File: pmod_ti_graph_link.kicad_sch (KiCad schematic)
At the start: 11 parts, among them J1 Pmod Peripheral, J2 Graph Link, J3 Link Debug, Q1 UMH4N

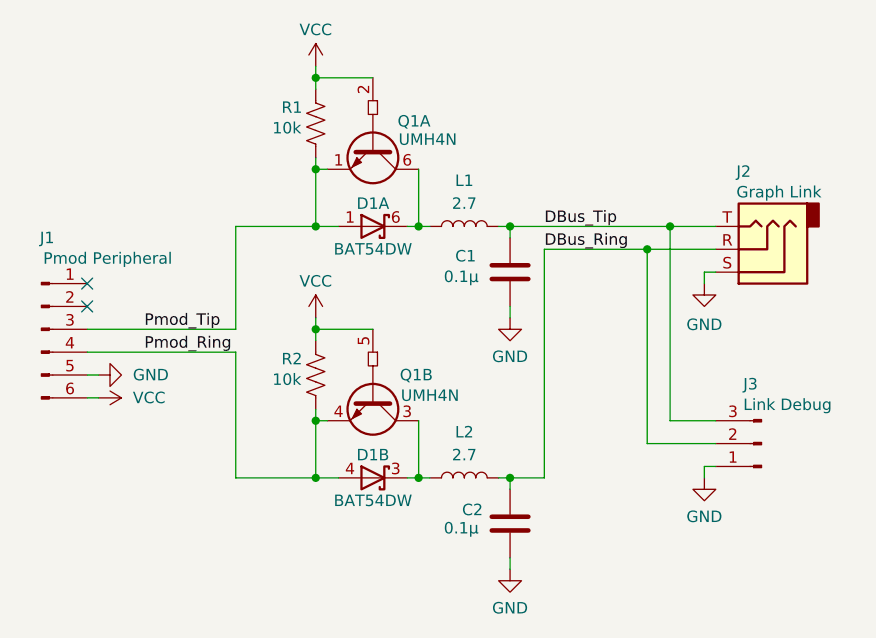
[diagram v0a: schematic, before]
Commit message: Clean up routing, add GND vias, add text
- Clean up routing around transistor and diode
- Add stitching GND vias around perimeter
- Add "Pmod TI Graph Link" text and date
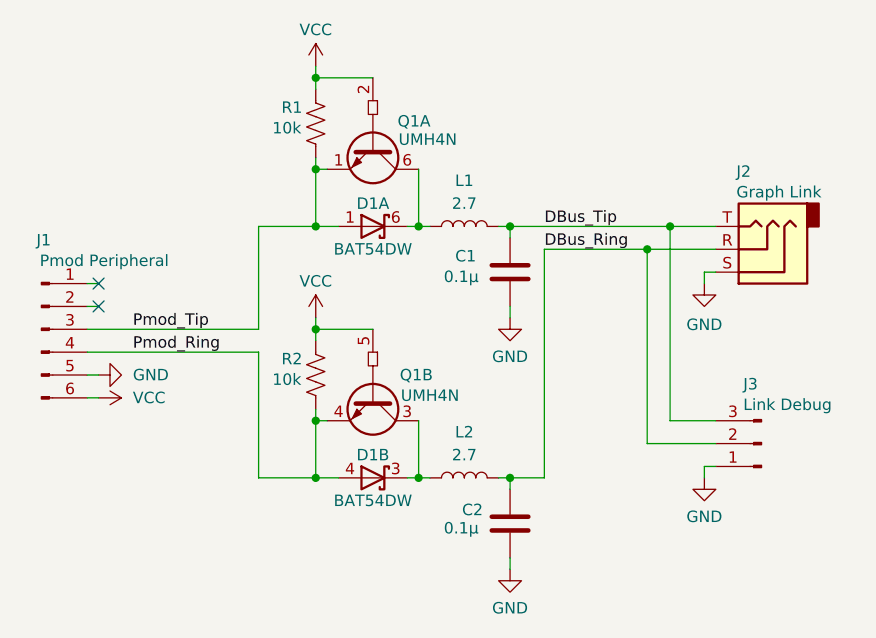
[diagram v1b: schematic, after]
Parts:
- added unit 2 of D1
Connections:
- net Pmod_Ring: now also D1.4 (A); no longer D1.4 (A)
- net at L2.1, Q1.3 (C2): now also D1.3 (K); no longer D1.3 (K)
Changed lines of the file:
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@@
 	)
 	(no_connect
-		(at 68.58 90.17)
+		(at 69.85 87.63)
 	)
 	(no_connect
-		(at 68.58 87.63)
+		(at 69.85 90.17)
 	)
 	(wire
@@
 	(wire
 		(pts
-			(xy 85.09 95.25) (xy 85.09 109.22)
+			(xy 87.63 95.25) (xy 87.63 109.22)
 		)
 		(stroke
@@
 	(wire
 		(pts
-			(xy 68.58 95.25) (xy 85.09 95.25)
+			(xy 68.58 95.25) (xy 87.63 95.25)
 		)
 		(stroke
@@
 	(wire
 		(pts
-			(xy 68.58 92.71) (xy 85.09 92.71)
+			(xy 68.58 92.71) (xy 87.63 92.71)
 		)
 		(stroke
@@
 	(wire
 		(pts
-			(xy 85.09 92.71) (xy 85.09 81.28)
+			(xy 87.63 92.71) (xy 87.63 81.28)
 		)
 		(stroke
@@
 	(wire
 		(pts
-			(xy 85.09 81.28) (xy 93.98 81.28)
+			(xy 87.63 81.28) (xy 93.98 81.28)
 		)
 		(stroke
@@
 	(wire
 		(pts
+			(xy 68.58 87.63) (xy 69.85 87.63)
+		)
+		(stroke
+			(width 0)
+			(type default)
+		)
+	)
+	(wire
+		(pts
 			(xy 137.16 107.95) (xy 137.16 109.22)
 		)
@@
 	(wire
 		(pts
-			(xy 85.09 109.22) (xy 93.98 109.22)
+			(xy 87.63 109.22) (xy 93.98 109.22)
 		)
 		(stroke
@@
 	(wire
 		(pts
+			(xy 68.58 90.17) (xy 69.85 90.17)
+		)
+		(stroke
+			(width 0)
+			(type default)
+		)
+	)
+	(wire
+		(pts
 			(xy 93.98 73.66) (xy 93.98 74.93)
 		)
@@
 	)
 	(label "Pmod_Ring"
-		(at 74.93 95.25 0)
+		(at 73.66 95.25 0)
 		(effects
 			(font
@@
 	)
 	(label "Pmod_Tip"
-		(at 74.93 92.71 0)
+		(at 73.66 92.71 0)
 		(effects
 			(font
@@
 		(dnp no)
 		(property "Reference" "J1"
-			(at 64.135 82.55 0)
+			(at 63.754 82.804 0)
 			(effects
 				(font
@@
 		)
 		(property "Value" "Pmod Peripheral"
-			(at 70.866 84.836 0)
-			(effects
-				(font
+			(at 70.485 85.09 0)
+			(effects
+				(font

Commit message: Add inductor shield->GND and clean up placement and routing. Prelim "Rev A"
- Add optional inductor between 2.5mm shield and GND
- Make VCC thicker, update calc icon, clean up traces
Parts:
- added L3: 2.7, Inductor_SMD:L_1008_2520Metric_Pad1.43x2.20mm_HandSolder, symbol Device:L
- Q1: value UMH4N -> RN1911
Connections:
- net GND: now also L3.1; no longer J2.S
- new net: J2.S, L3.2
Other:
- moved on the sheet: J3
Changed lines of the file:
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@@
 	(wire
 		(pts
-			(xy 133.35 102.87) (xy 133.35 81.28)
+			(xy 133.35 107.95) (xy 133.35 81.28)
 		)
 		(stroke
@@
 	(wire
 		(pts
-			(xy 137.16 107.95) (xy 138.43 107.95)
+			(xy 137.16 113.03) (xy 138.43 113.03)
 		)
 		(stroke
@@
 	(wire
 		(pts
-			(xy 130.81 83.82) (xy 130.81 105.41)
+			(xy 130.81 83.82) (xy 130.81 110.49)
 		)
 		(stroke
@@
 	(wire
 		(pts
+			(xy 137.16 86.36) (xy 137.16 87.63)
+		)
+		(stroke
+			(width 0)
+			(type default)
+		)
+	)
+	(wire
+		(pts
 			(xy 93.98 81.28) (xy 96.52 81.28)
 		)
@@
 	(wire
 		(pts
-			(xy 137.16 107.95) (xy 137.16 109.22)
+			(xy 137.16 113.03) (xy 137.16 114.3)
 		)
 		(stroke
@@
 	(wire
 		(pts
+			(xy 137.16 95.25) (xy 137.16 96.52)
+		)
+		(stroke
+			(width 0)
+			(type default)
+		)
+	)
+	(wire
+		(pts
 			(xy 93.98 64.77) (xy 100.33 64.77)
 		)
@@
 	(wire
 		(pts
-			(xy 133.35 102.87) (xy 138.43 102.87)
-		)
-		(stroke
-			(width 0)
-			(type default)
-		)
-	)
-	(wire
-		(pts
-			(xy 130.81 105.41) (xy 138.43 105.41)
-		)
-		(stroke
-			(width 0)
-			(type default)
-		)
-	)
-	(wire
-		(pts
-			(xy 137.16 87.63) (xy 137.16 86.36)
+			(xy 133.35 107.95) (xy 138.43 107.95)
+		)
+		(stroke
+			(width 0)
+			(type default)
+		)
+	)
+	(wire
+		(pts
+			(xy 130.81 110.49) (xy 138.43 110.49)
 		)
 		(stroke
@@
 	(symbol
 		(lib_id "power:GND")
-		(at 137.16 109.22 0)
+		(at 137.16 114.3 0)
 		(unit 1)
 		(exclude_from_sim no)
@@
 		(dnp no)
 		(property "Reference" "#PWR06"
-			(at 137.16 115.57 0)
+			(at 137.16 120.65 0)
 			(effects
 				(font
@@
 		)
 		(property "Value" "GND"
-			(at 137.16 113.538 0)
+			(at 137.16 118.618 0)
 			(effects
 				(font
@@
 		)
 		(property "Footprint" ""
-			(at 137.16 109.22 0)
+			(at 137.16 114.3 0)
 			(effects
 				(font
@@
 		)
 		(property "Datasheet" ""
-			(at 137.16 109.22 0)
+			(at 137.16 114.3 0)
 			(effects
 				(font
@@
 		)
 		(property "Description" "Power symbol creates a global label with name \"GND\" , ground"
-			(at 137.16 109.22 0)
+			(at 137.16 114.3 0)
 			(effects
 				(font
@@
 				(path "/d64bf880-8167-432e-9a3f-0e567d00bae5"
 					(reference "#PWR06")
+					(unit 1)
+				)
+			)
+		)
+	)
+	(symbol
+		(lib_id "Device:L")
+		(at 137.16 91.44 180)
+		(unit 1)
+		(exclude_from_sim no)
+		(in_bom yes)
+		(on_board yes)
+		(dnp no)
+		(fields_autoplaced yes)
+		(property "Reference" "L3"
+			(at 138.43 90.1699 0)
+			(effects
+				(font
+					(size 1.27 1.27)
+				)
+				(justify right)
+			)
+		)
+		(property "Value" "2.7"
+			(at 138.43 92.7099 0)
+			(effects
+				(font
+					(size 1.27 1.27)
+				)
+				(justify right)
+			)
+		)
+		(property "Footprint" "Inductor_SMD:L_1008_2520Metric_Pad1.43x2.20mm_HandSolder"
+			(at 137.16 91.44 0)
+			(effects
+				(font
+					(size 1.27 1.27)
+				)
+				(hide yes)
+			)
+		)
+		(property "Datasheet" "~"
+			(at 137.16 91.44 0)
+			(effects
+				(font
+					(size 1.27 1.27)
+				)
+				(hide yes)
+			)
+		)
+		(property "Description" "Inductor"
+			(at 137.16 91.44 0)
+			(effects
+				(font
+					(size 1.27 1.27)
+				)
+				(hide yes)
+			)
+		)
+		(pin "1"
+		)
+		(pin "2"
+		)
+		(instances
+			(project "pmod_ti_graph_link"
+				(path "/d64bf880-8167-432e-9a3f-0e567d00bae5"
+					(reference "L3")
 					(unit 1)
 				)
@@
 	(symbol
 		(lib_id "power:GND")
-		(at 137.16 87.63 0)
+		(at 137.16 96.52 0)
 		(unit 1)
 		(exclude_from_sim no)
@@
 		(dnp no)
 		(property "Reference" "#PWR05"
-			(at 137.16 93.98 0)
+			(at 137.16 102.87 0)
 			(effects
 				(font
@@
 		)
 		(property "Value" "GND"
-			(at 137.16 92.202 0)
+			(at 137.16 101.092 0)
 			(effects
 				(font
@@
 		)
 		(property "Footprint" ""
-			(at 137.16 87.63 0)
+			(at 137.16 96.52 0)
 			(effects
 				(font
@@
 		)
 		(property "Datasheet" ""
-			(at 137.16 87.63 0)
+			(at 137.16 96.52 0)
 			(effects
 				(font
@@
 		)
 		(property "Description" "Power symbol creates a global label with name \"GND\" , ground"
-			(at 137.16 87.63 0)
+			(at 137.16 96.52 0)
 			(effects
 				(font
@@
 			)
 		)
-		(property "Value" "UMH4N"
+		(property "Value" "RN1911"
 			(at 106.68 100.076 90)
 			(effects
@@
 			)
 		)
-		(property "Value" "UMH4N"
+		(property "Value" "RN1911"
 			(at 106.426 71.628 90)
 			(effects
@@
 	(symbol
 		(lib_id "Connector:Conn_01x03_Pin")
-		(at 143.51 105.41 180)
+		(at 143.51 110.49 180)
 		(unit 1)
 		(exclude_from_sim no)
@@
 		(dnp no)
 		(property "Reference" "J3"
-			(at 141.478 98.806 0)
+			(at 141.478 103.886 0)
 			(effects
 				(font
@@
 		)
 		(property "Value" "Link Debug"
-			(at 141.478 101.092 0)
+			(at 141.478 106.172 0)
 			(effects
 				(font
@@
 		)
 		(property "Footprint" "Connector_PinHeader_2.54mm:PinHeader_1x03_P2.54mm_Vertical"
-			(at 143.51 105.41 0)
+			(at 143.51 110.49 0)
 			(effects
 				(font
@@
 		)
 		(property "Datasheet" "~"
-			(at 143.51 105.41 0)
+			(at 143.51 110.49 0)
 			(effects
 				(font
@@
 		)
 		(property "Description" "Generic connector, single row, 01x03, script generated"
-			(at 143.51 105.41 0)
-			(effects
-				(font
+			(at 143.51 110.49 0)
+			(effects
+				(font

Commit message: Add part numbers, README, and images of schematic/PCB/model
- Add README detailing the project scope and BOM
- Add image with screenshot of schematic, PCB, and 3D model
- Specify solder mask and ENIG finish
- Add Digikey part numbers for reference
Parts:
- C1, C2: Digikey (none) -> 311-1140-1-ND
- D1: value BAT54DW -> BAT54DW_R1_00001; Digikey (none) -> 3757-BAT54DW_R1_00001CT-ND
- J1: Digikey (none) -> 1849-PR20206HBNN-ND
- J2: Digikey (none) -> 2092-STX-2500-3NTRCT-ND
- J3: Digikey (none) -> 1849-1003-ND
- L1, L2, L3: Digikey (none) -> 445-16474-1-ND
- Q1: Digikey (none) -> RN1911LF(CTCT-ND
- R1, R2: Digikey (none) -> 13-RC0805JR-1310KLCT-ND
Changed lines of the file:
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@@
 			)
 		)
-		(property "Datasheet" "~"
+		(property "Datasheet" "https://product.tdk.com/en/system/files?file=dam/doc/product/inductor/inductor/smd/catalog/inductor_commercial_standard_nlv25-ef_en.pdf"
 			(at 137.16 91.44 0)
 			(effects
@@
 			)
 		)
+		(property "Digikey" "445-16474-1-ND"
+			(at 137.16 91.44 0)
+			(effects
+				(font
+					(size 1.27 1.27)
+				)
+				(hide yes)
+			)
+		)
 		(pin "1"
 		)
@@
 			)
 		)
-		(property "Datasheet" "~"
+		(property "Datasheet" "https://www.yageo.com/upload/media/product/productsearch/datasheet/mlcc/UPY-GPHC_X7R_6.3V-to-250V_24.pdf"
 			(at 115.57 114.3 0)
 			(effects
@@
 		)
 		(property "Description" "Unpolarized capacitor"
+			(at 115.57 114.3 0)
+			(effects
+				(font
+					(size 1.27 1.27)
+				)
+				(hide yes)
+			)
+		)
+		(property "Digikey" "311-1140-1-ND"
 			(at 115.57 114.3 0)
 			(effects
@@
 			)
 		)
-		(property "Datasheet" "~"
+		(property "Datasheet" "https://product.tdk.com/en/system/files?file=dam/doc/product/inductor/inductor/smd/catalog/inductor_commercial_standard_nlv25-ef_en.pdf"
 			(at 110.49 109.22 0)
 			(effects
@@
 			)
 		)
+		(property "Digikey" "445-16474-1-ND"
+			(at 110.49 109.22 90)
+			(effects
+				(font
+					(size 1.27 1.27)
+				)
+				(hide yes)
+			)
+		)
 		(pin "1"
 		)
@@
 			)
 		)
-		(property "Datasheet" "~"
+		(property "Datasheet" "https://www.yageogroup.com/content/datasheet/asset/file/PYU-RC_GROUP_51_ROHS_L"
 			(at 93.98 97.79 0)
 			(effects
@@
 			)
 		)
+		(property "Digikey" "13-RC0805JR-1310KLCT-ND"
+			(at 93.98 97.79 0)
+			(effects
+				(font
+					(size 1.27 1.27)
+				)
+				(hide yes)
+			)
+		)
 		(pin "1"
 		)
@@
 			)
 		)
-		(property "Datasheet" "~"
+		(property "Datasheet" "https://www.yageogroup.com/content/datasheet/asset/file/PYU-RC_GROUP_51_ROHS_L"
 			(at 93.98 69.85 0)
 			(effects
@@
 		)
 		(property "Description" "Resistor, US symbol"
+			(at 93.98 69.85 0)
+			(effects
+				(font
+					(size 1.27 1.27)
+				)
+				(hide yes)
+			)
+		)
+		(property "Digikey" "13-RC0805JR-1310KLCT-ND"
 			(at 93.98 69.85 0)
 			(effects
@@
 			)
 		)
-		(property "Datasheet" "http://rohmfs.rohm.com/en/products/databook/datasheet/discrete/transistor/digital/emh3t2r-e.pdf"
+		(property "Datasheet" "https://toshiba.semicon-storage.com/info/RN1911_datasheet_ja_20210824.pdf?did=18827&prodName=RN1911"
 			(at 100.33 105.41 0)
 			(effects
@@
 		(property "Description" "0.1A Ic, 50V Vce, Dual NPN Input Resistor Transistors, SOT-363"
 			(at 100.33 101.6 0)
+			(effects
+				(font
+					(size 1.27 1.27)
+				)
+				(hide yes)
+			)
+		)
+		(property "Digikey" "RN1911LF(CTCT-ND"
+			(at 100.33 101.6 90)
 			(effects
 				(font
@@
 			)
 		)
-		(property "Datasheet" "http://rohmfs.rohm.com/en/products/databook/datasheet/discrete/transistor/digital/emh3t2r-e.pdf"
+		(property "Datasheet" "https://toshiba.semicon-storage.com/info/RN1911_datasheet_ja_20210824.pdf?did=18827&prodName=RN1911"
 			(at 100.33 77.47 0)
 			(effects
@@
 			)
 		)
+		(property "Digikey" "RN1911LF(CTCT-ND"
+			(at 100.33 73.66 90)
+			(effects
+				(font
+					(size 1.27 1.27)
+				)
+				(hide yes)
+			)
+		)
 		(pin "5"
 		)
@@
 			)
 		)
-		(property "Value" "BAT54DW"
+		(property "Value" "BAT54DW_R1_00001"
 			(at 100.33 83.82 0)
 			(effects
@@
 			)
 		)
-		(property "Datasheet" ""
+		(property "Datasheet" "https://www.panjit.com.tw/upload/datasheet/BAT54TW_SERIES.pdf"
 			(at 100.33 81.28 0)
 			(effects
@@
 			)
 		)
-		(property "Description" ""
+		(property "Description" "Schottky diode array 30V 200mA SOT363"
+			(at 100.33 81.28 0)
+			(effects
+				(font
+					(size 1.27 1.27)
+				)
+				(hide yes)
+			)
+		)
+		(property "Digikey" "3757-BAT54DW_R1_00001CT-ND"
 			(at 100.33 81.28 0)
 			(effects
@@
 			)
 		)
-		(property "Value" "BAT54DW"
+		(property "Value" "BAT54DW_R1_00001"
 			(at 100.33 111.76 0)
 			(effects
@@
 			)
 		)
-		(property "Datasheet" ""
+		(property "Datasheet" "https://www.panjit.com.tw/upload/datasheet/BAT54TW_SERIES.pdf"
 			(at 100.33 109.22 0)
 			(effects
@@
 			)
 		)
-		(property "Description" ""
+		(property "Description" "Schottky diode array 30V 200mA SOT363"
+			(at 100.33 109.22 0)
+			(effects
+				(font
+					(size 1.27 1.27)
+				)
+				(hide yes)
+			)
+		)
+		(property "Digikey" "3757-BAT54DW_R1_00001CT-ND"
 			(at 100.33 109.22 0)
 			(effects
@@
 			)
 		)
-		(property "Datasheet" "~"
+		(property "Datasheet" "https://www.kycon.com/Pub_Eng_Draw/STX-2500-3N.pdf"
 			(at 143.51 83.82 0)
 			(effects
@@
 		)
 		(property "Description" "Audio Jack, 3 Poles (Stereo / TRS)"
+			(at 143.51 83.82 0)
+			(effects
+				(font
+					(size 1.27 1.27)
+				)
+				(hide yes)
+			)
+		)
+		(property "Digikey" "2092-STX-2500-3NTRCT-ND"
 			(at 143.51 83.82 0)
 			(effects
@@
 			)
 		)
-		(property "Datasheet" "~"
+		(property "Datasheet" "https://product.tdk.com/en/system/files?file=dam/doc/product/inductor/inductor/smd/catalog/inductor_commercial_standard_nlv25-ef_en.pdf"
 			(at 110.49 81.28 0)
 			(effects
@@
 			)
 		)
+		(property "Digikey" "445-16474-1-ND"
+			(at 110.49 81.28 90)
+			(effects
+				(font
+					(size 1.27 1.27)
+				)
+				(hide yes)
+			)
+		)
 		(pin "1"
 		)
@@
 			)
 		)
-		(property "Datasheet" "~"
+		(property "Datasheet" "https://www.yageo.com/upload/media/product/productsearch/datasheet/mlcc/UPY-GPHC_X7R_6.3V-to-250V_24.pdf"
 			(at 115.57 86.36 0)
 			(effects
@@
 			)
 		)
+		(property "Digikey" "311-1140-1-ND"
+			(at 115.57 86.36 0)
+			(effects
+				(font
+					(size 1.27 1.27)
+				)
+				(hide yes)
+			)
+		)
 		(pin "1"
 		)
@@
 			)
 		)
-		(property "Datasheet" "~"
+		(property "Datasheet" "https://media.metz-connect.com/files/171/Data_sheet_PR202XXVBNN.PDF"
 			(at 143.51 110.49 0)
 			(effects
@@
 			)
 		)
+		(property "Digikey" "1849-1003-ND"
+			(at 143.51 110.49 0)
+			(effects
+				(font
+					(size 1.27 1.27)
+				)
+				(hide yes)
+			)
+		)
 		(pin "2"
 		)
@@
 			)
 		)
-		(property "Datasheet" "~"
+		(property "Datasheet" "https://media.metz-connect.com/files/171/Data_sheet_PR202XXHBNN.PDF"
 			(at 63.5 92.71 0)
 			(effects
@@
 			(at 63.5 92.71 0)
 			(effects
+				(font
+					(size 1.27 1.27)
+				)
+				(hide yes)
+			)
+		)
+		(property "Digikey" "1849-PR20206HBNN-ND"
+			(at 63.5 92.71 0)
+			(effects
